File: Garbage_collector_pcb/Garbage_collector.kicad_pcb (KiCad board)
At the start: 4 copper layers, 86.9 x 52.9 mm, 110 parts, among them J1 NRF52840, J10 Lidar, J11 VL53L0CXV0DH1, J12 NEOPIXELS, J2 Conn_ST_STDC14, J3 USB_C_Receptacle_PowerOnly_6P, J4 MOTOR2, J5 MOTOR1, J6 SERVO1, J7 SERVO2, J8 VL53L0CXV0DH1, J9 ADA3595, Q1 MMDT2907A-7-F, Q2 DMP1045U-7, Q3 DMN313DLT-7, SW1 SW_Push, SW2 SW_Push, U1 STM32G431RBTx, U2 BQ27220YZFR, U3 BQ25896RTWR, U4 DRV8833PWP, U5 SN74AHCT1G125DBVR, Y1 16MHz

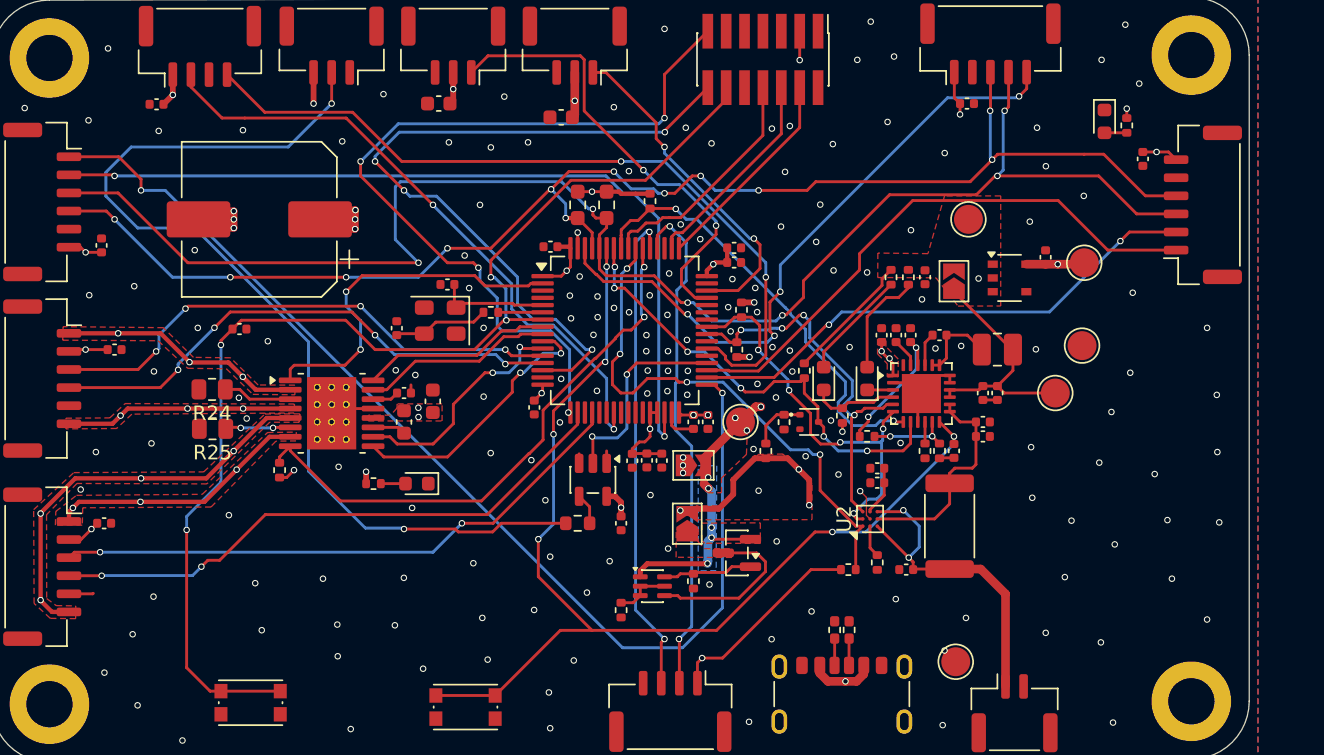
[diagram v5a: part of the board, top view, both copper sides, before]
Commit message: ajout noms connecteurs + pins + noms membres de l'equipe (F.Silkscreen)
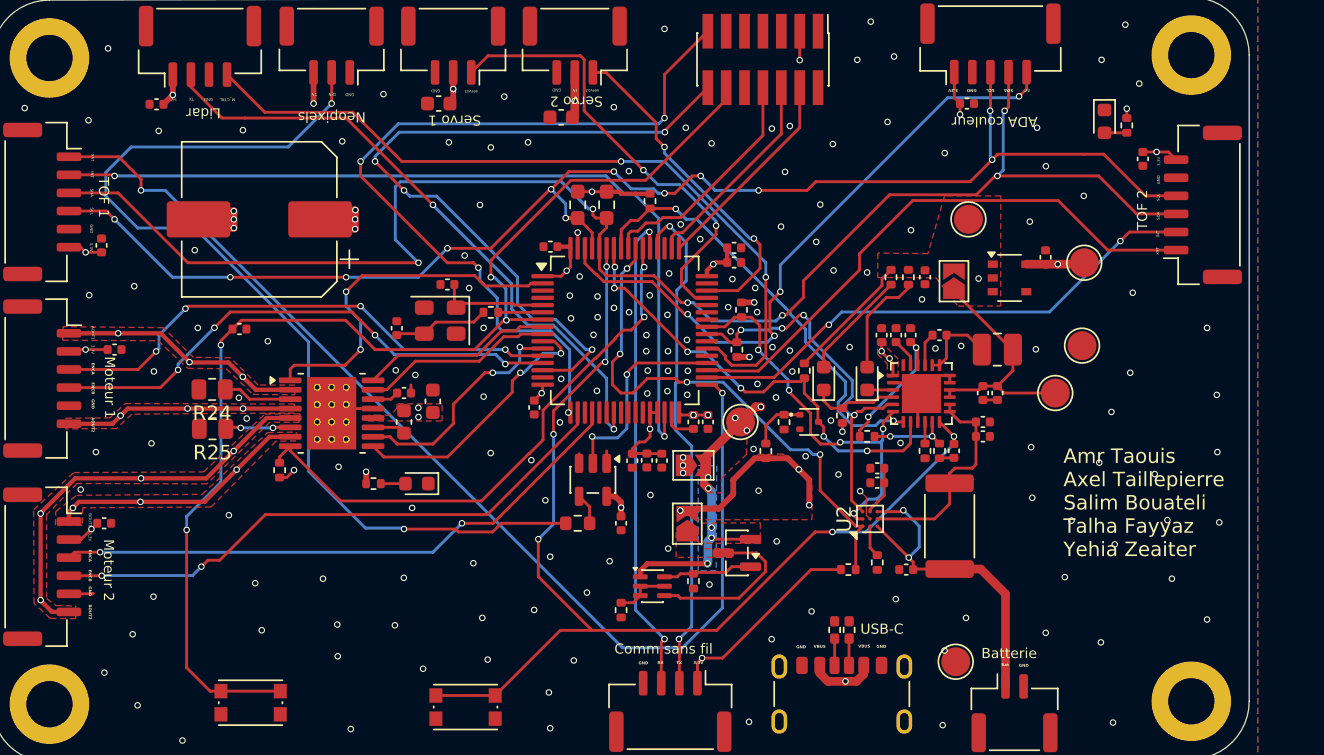
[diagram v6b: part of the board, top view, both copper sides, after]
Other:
- board text added: "3,3V"
- board text added: "5V"
- board text added: "ADA couleur"
- board text added: "AOUT1"
- board text added: "AOUT2"
- board text added: "Amr Taouis Axel Taillepierre Salim Bouateli Talha Fayyaz Yehia Zeaiter"
- board text added: "BOUT1"
- board text added: "BOUT2"
- board text added: "Bat"
- board text added: "Batterie"
- board text added: "Comm sans fil"
- board text added: "DIN"
- board text added: "ENCA"
- board text added: "ENCB"
- board text added: "GND"
- board text added: "INT"
- board text added: "Lidar"
- board text added: "M_CTRL"
- board text added: "Moteur 1"
- board text added: "Moteur 2"
- board text added: "Neopixels"
- board text added: "RX"
- board text added: "SCL"
- board text added: "SDA"
- board text added: "Servo 1"
- board text added: "Servo 2"
- board text added: "TOF 1"
- board text added: "TOF 2"
- board text added: "TX"
- board text added: "USB-C"
- board text added: "VBUS"
- board text added: "XST"
- board text added: "servo1"
- board text added: "servo2"
